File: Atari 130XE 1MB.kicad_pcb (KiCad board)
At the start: 2 copper layers, 324 x 204 mm, 348 parts, among them J1 SIO, J10 Mem_on_off, J100 cond, J101 cond, J102 pin, J103 pin, J104 pin, J105 pin, J106 pin, J107 pin, J2 Video, J201 Diagnostic, J202 Diag, J210 Diag, J211 Conn_01x02, J24 Cartridge, J4 Expansion, J5 Joystick_Port, J6 Joystick_Port, J7 Power, J8 Keyboard, M1 Modulator, Q1 2N3904, Q2 2N3904, Q3 2N3904, Q4 2N3906, Q6 2N3904, SW1 Switch_power_on, U1 LM358, U10 DRAM_4464, U100 74LS157, U17 GTIA, U18 74LS08, U19 LM555, U2 74LS138, U20 4050, U21 74LS74, U22 POKEY, U23 PIA, U24 CD4051B, U25 CD4051B, U3 MMU, U4 27C010, U40 GAL20V8_DIP, U41 74LS157, U42 74LS175, U43 DRAM_1MB_4bit, U44 DRAM_1MB_4bit, U5 27C010, U6 Freddie, U7 Antic, U8 Sally, U9 DRAM_4464, Y1 Crystal, Y2 4,43 MHz

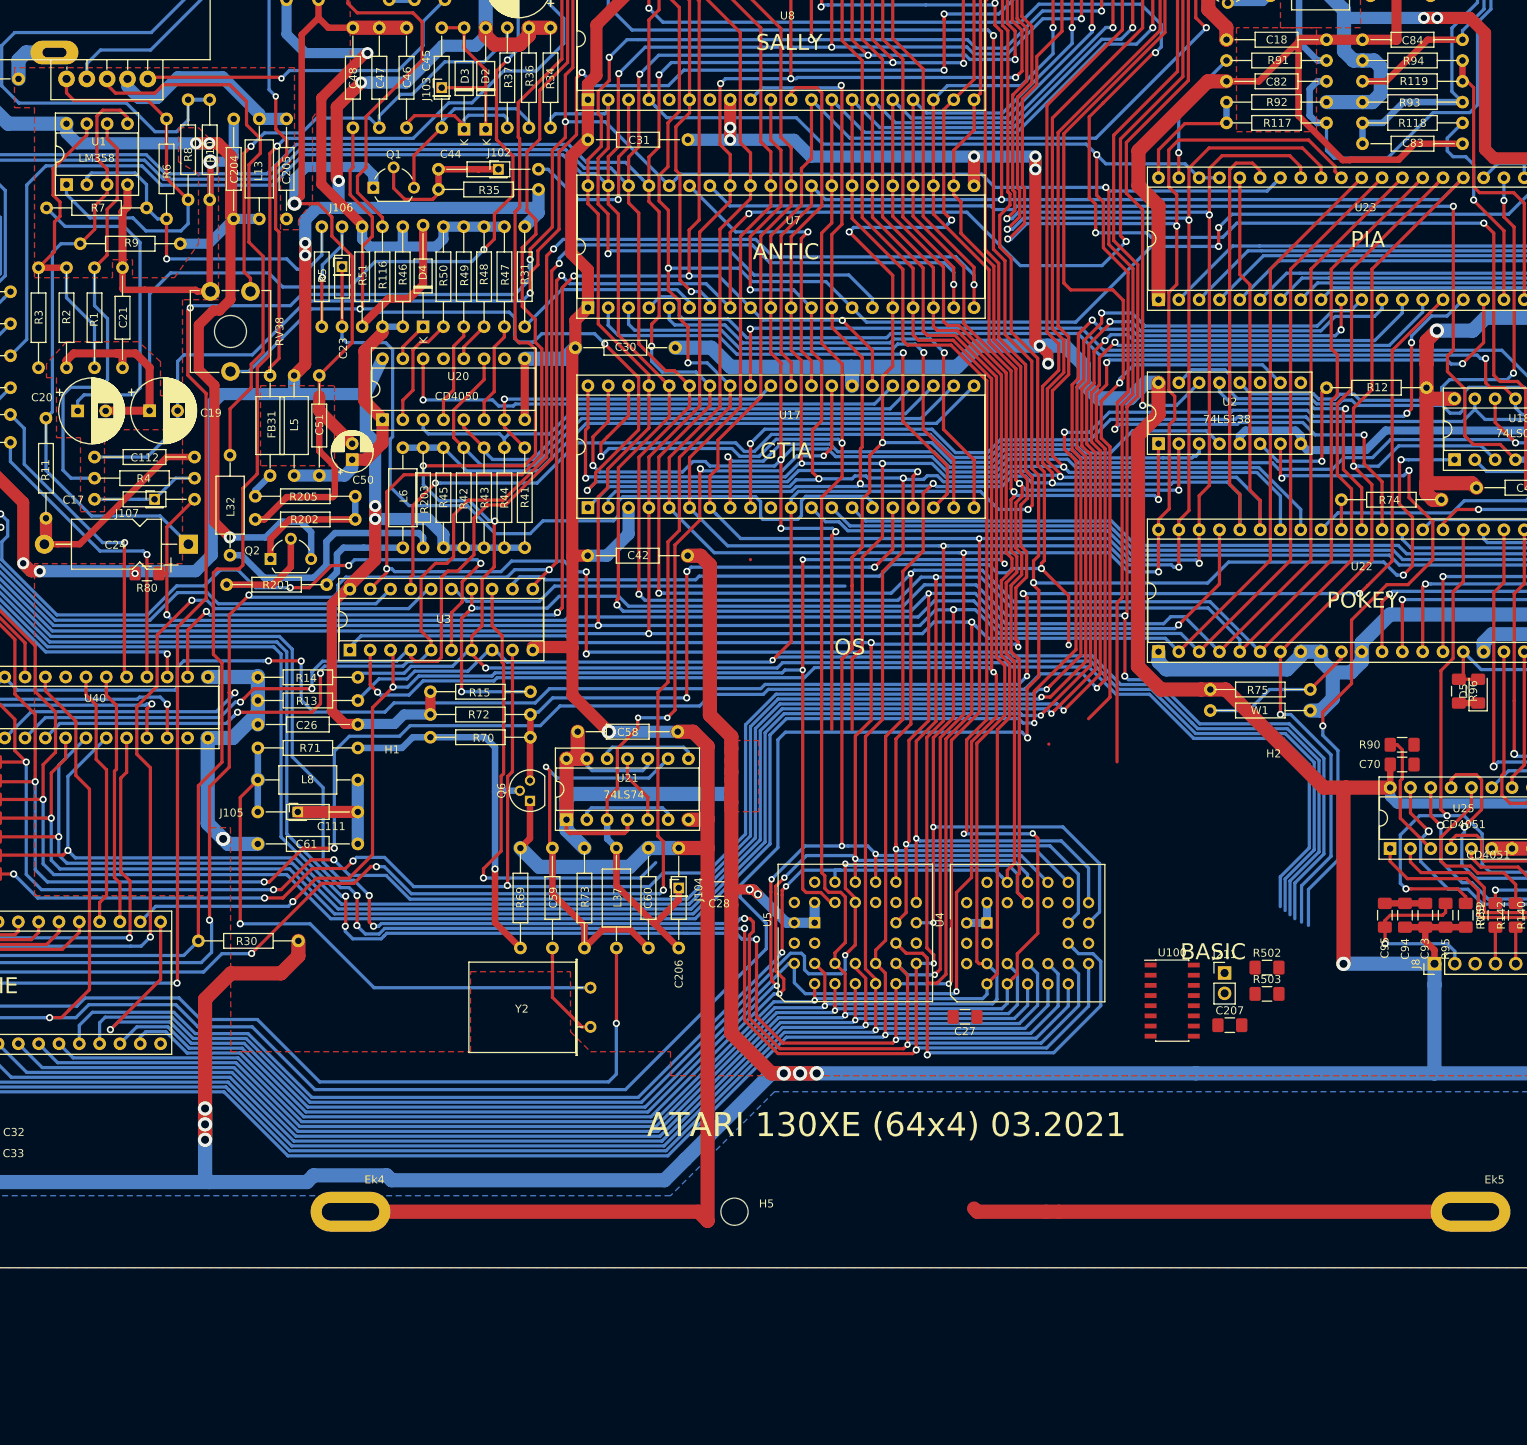
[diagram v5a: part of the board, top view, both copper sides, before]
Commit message: Add Basci and SO PLCC
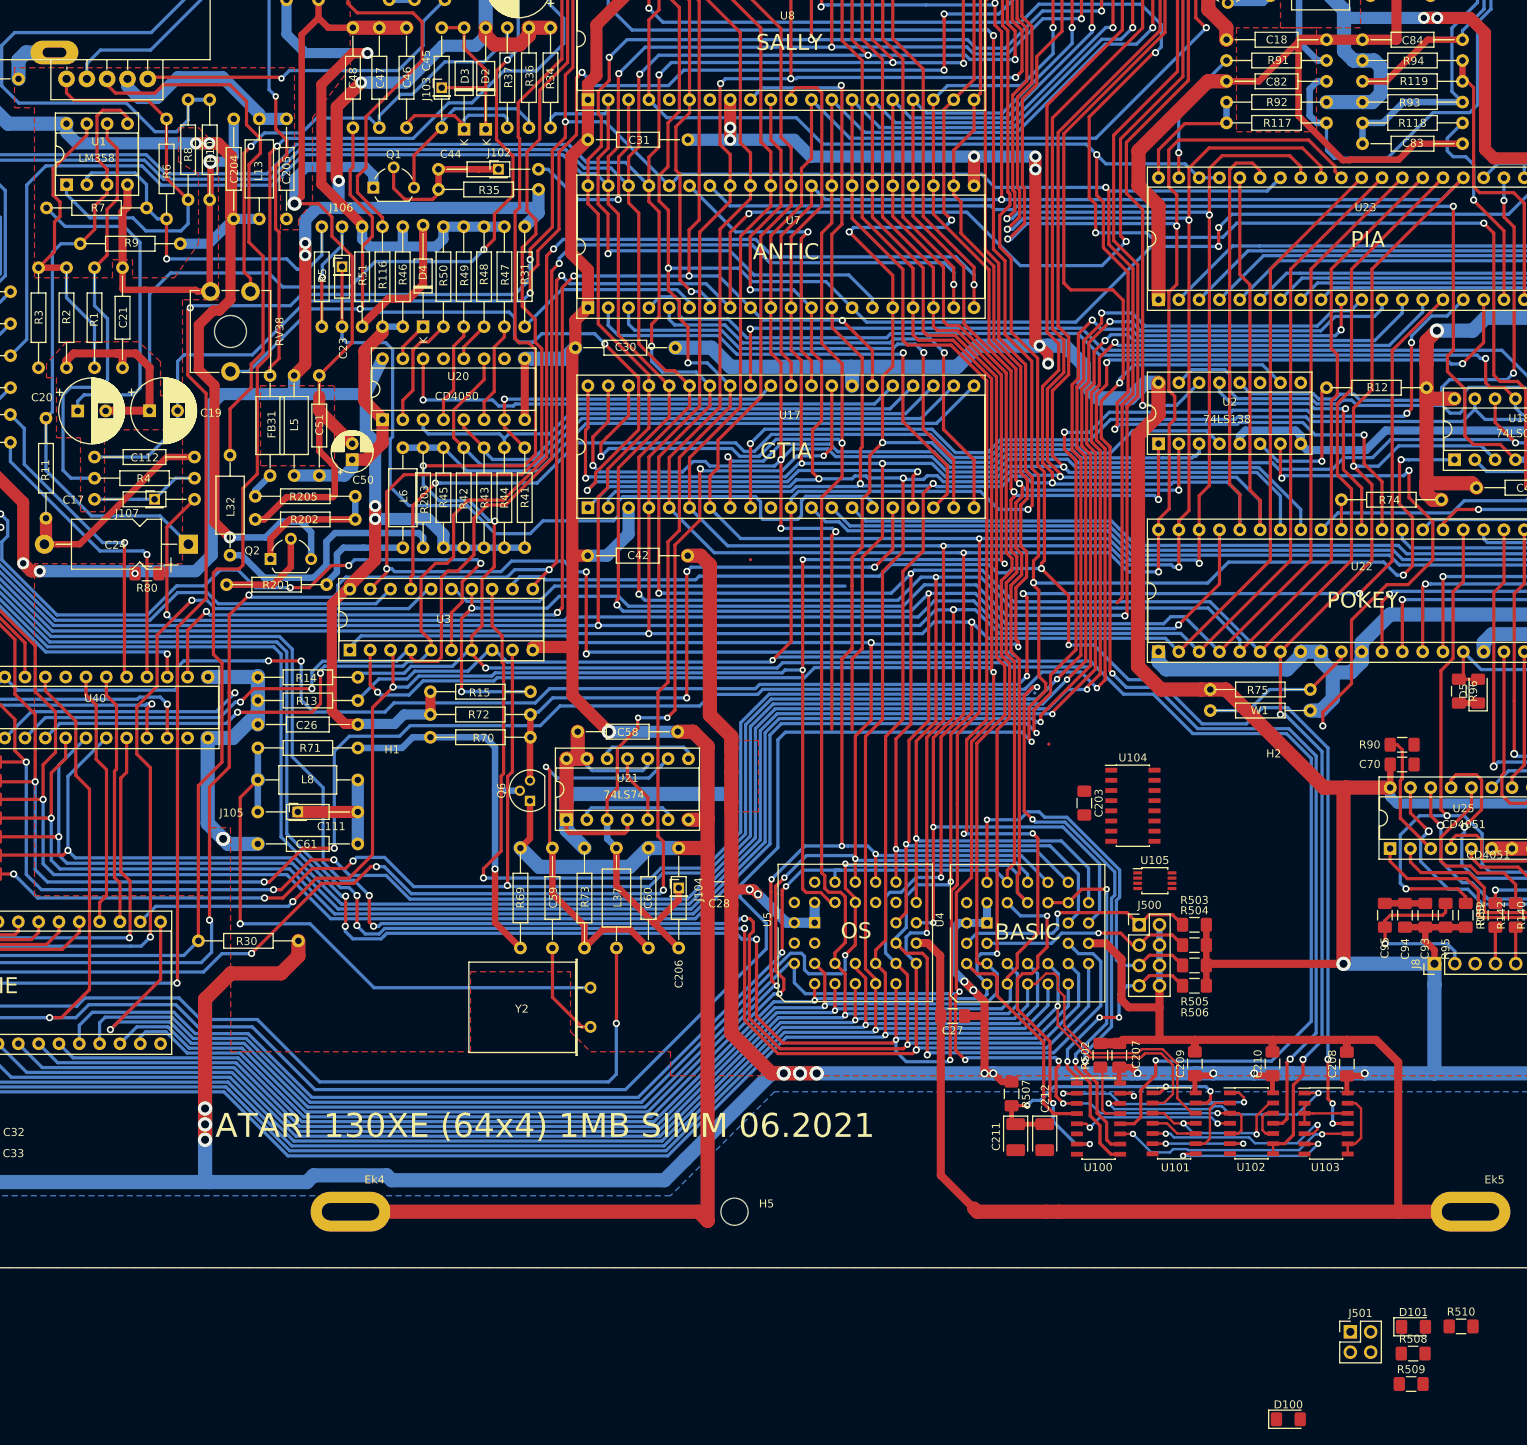
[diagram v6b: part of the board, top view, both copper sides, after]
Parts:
- removed J211: Conn_01x02, Connector_PinHeader_2.54mm:PinHeader_1x02_P2.54mm_Vertical
- added C203: 1uF, Capacitor_SMD:C_1206_3216Metric_Pad1.42x1.75mm_HandSolder, F.Cu at (240.6, 188.8)
- added C208: 100nF, Capacitor_SMD:C_1206_3216Metric_Pad1.42x1.75mm_HandSolder, F.Cu at (273.4, 221.4)
- added C209: 100nF, Capacitor_SMD:C_1206_3216Metric_Pad1.42x1.75mm_HandSolder, F.Cu at (254.4, 221.4)
- added C210: 100nF, Capacitor_SMD:C_1206_3216Metric_Pad1.42x1.75mm_HandSolder, F.Cu at (264.1, 221.4)
- added C211: 22uF, Capacitor_Tantalum_SMD:CP_EIA-3528-21_Kemet-B_Pad1.50x2.35mm_HandSolder, F.Cu at (232.0, 230.6)
- added C212: 4u7, Capacitor_Tantalum_SMD:CP_EIA-3528-21_Kemet-B_Pad1.50x2.35mm_HandSolder, F.Cu at (235.7, 230.6)
- added D100: 1N4148, Diode_SMD:D_1206_3216Metric_Pad1.42x1.75mm_HandSolder, F.Cu at (266.1, 265.8)
- added D101: 1N4148, Diode_SMD:D_1206_3216Metric_Pad1.42x1.75mm_HandSolder, F.Cu at (281.8, 254.3)
- added J500: Basic_sel, Connector_PinHeader_2.54mm:PinHeader_2x04_P2.54mm_Vertical, F.Cu at (247.5, 204.0)
- added J501: TPP_sel, Connector_PinHeader_2.54mm:PinHeader_2x02_P2.54mm_Vertical, F.Cu at (273.9, 254.9)
- added R504: 10k, Resistor_SMD:R_1206_3216Metric_Pad1.42x1.75mm_HandSolder, F.Cu at (254.4, 206.6)
- added R505: 10k, Resistor_SMD:R_1206_3216Metric_Pad1.42x1.75mm_HandSolder, F.Cu at (254.4, 209.1)
- added R506: 10k, Resistor_SMD:R_1206_3216Metric_Pad1.42x1.75mm_HandSolder, F.Cu at (254.4, 211.6)
- added R507: 1k2, Resistor_SMD:R_1206_3216Metric_Pad1.42x1.75mm_HandSolder, F.Cu at (231.5, 225.1)
- added R508: 4k7, Resistor_SMD:R_1206_3216Metric_Pad1.42x1.75mm_HandSolder, F.Cu at (281.7, 257.6)
- added R509: 4k7, Resistor_SMD:R_1206_3216Metric_Pad1.42x1.75mm_HandSolder, F.Cu at (281.5, 261.4)
- added R510: 10k, Resistor_SMD:R_1206_3216Metric_Pad1.42x1.75mm_HandSolder, F.Cu at (287.7, 254.2)
- added U101: 74LS74, Package_SO:SOIC-14_3.9x8.7mm_P1.27mm, F.Cu at (251.8, 228.8)
- added U102: 74HC02, Package_SO:SOIC-14_3.9x8.7mm_P1.27mm, F.Cu at (261.5, 228.8)
- added U103: 74HC02, Package_SO:SOIC-14_3.9x8.7mm_P1.27mm, F.Cu at (270.8, 228.9)
- added U104: 74LS157, Package_SO:SOIC-16_3.9x9.9mm_P1.27mm, F.Cu at (246.7, 189.1)
- added U105: 74LVC2G74, Package_SO:TSSOP-8_3x3mm_P0.65mm, F.Cu at (249.4, 198.5)
- moved R502 23.5 mm to (242.6, 220.3), turned to 90 degrees
- moved U100 17.4 mm to (242.4, 228.2)
- moved C207 14.3 mm to (245.0, 220.3), turned to 90 degrees
- moved R503 12.5 mm to (254.4, 204.0), turned to 180 degrees
- moved C27 1.55 mm to (224.2, 215.4)
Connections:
- R503 pad 2: Net-(J211-Pad1) -> A16_sel
- U100 pad 1: Net-(J211-Pad1) -> Net-(J500-Pad7)
- U100 pad 11: (no net) -> Net-(U100-Pad11)
- U100 pad 12: (no net) -> RD5
- U100 pad 14: (no net) -> Net-(U100-Pad14)
- U100 pad 2: (no net) -> Net-(U100-Pad2)
- U100 pad 5: (no net) -> Net-(U100-Pad5)
- U100 pad 6: +5VA -> GND
- U2 pad 9: (no net) -> D6XX
- U4 pad 2: (no net) -> A16_sel
- U4 pad 29: (no net) -> A14_sel
- U4 pad 3: (no net) -> A15_sel
- U5 pad 2: (no net) -> Net-(U104-Pad12)
- U5 pad 29: (no net) -> Net-(U104-Pad7)
- U5 pad 3: (no net) -> Net-(U104-Pad9)
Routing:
- net BASIC: track 60.5 -> 194.3 mm, vias 1 -> 4
- net GND: track 1397.5 -> 1527.7 mm, vias 33 -> 34
- net S5: track 177.4 -> 265.9 mm, vias 3 -> 6
- net +5VA: track 1963.4 -> 2036.6 mm, vias 33 -> 41
- net CCTL: track 177.4 -> 249.3 mm, vias 4 -> 6
- net S4: track 360.5 -> 296.2 mm
- net MPD: track 332.8 -> 274.5 mm, vias 5 -> 4
- net A12: track 401.3 -> 456.7 mm, vias 5 -> 9
- net RD4: track 355.3 -> 303.4 mm
- net A14_sel: track 0.00 -> 48.8 mm, vias 0 -> 1
- net Net-(U100-Pad9): track 0.00 -> 45.8 mm, vias 0 -> 2
- net RD5: track 294.8 -> 339.4 mm, vias 5 -> 6
- net Net-(U100-Pad7): track 0.00 -> 42.8 mm, vias 0 -> 3
- net Net-(C211-Pad1): track 0.00 -> 37.3 mm, vias 0 -> 3
- net A3: track 432.1 -> 466.9 mm
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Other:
- board text added: "ATARI 130XE (64x4) 1MB SIMM 06.2021"
- board text removed: "ATARI 130XE (64x4) 03.2021"

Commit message: Final modification
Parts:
- added C160: 1n, Capacitor_SMD:C_1206_3216Metric_Pad1.42x1.75mm_HandSolder, F.Cu at (118.9, 83.9)
- added C99: 100nF, Capacitor_SMD:C_1206_3216Metric_Pad1.42x1.75mm_HandSolder, F.Cu at (246.3, 176.1)
- added J11: C, Connector_PinHeader_2.54mm:PinHeader_1x01_P2.54mm_Vertical, F.Cu at (69.7, 73.9)
- added J12: C, Connector_PinHeader_2.54mm:PinHeader_1x01_P2.54mm_Vertical, F.Cu at (69.7, 71.1)
- added J13: C, Connector_PinHeader_2.54mm:PinHeader_1x01_P2.54mm_Vertical, F.Cu at (69.7, 65.6)
- added J14: C, Connector_PinHeader_2.54mm:PinHeader_1x01_P2.54mm_Vertical, F.Cu at (82.9, 73.9)
- added J15: C, Connector_PinHeader_2.54mm:PinHeader_1x01_P2.54mm_Vertical, F.Cu at (82.9, 71.1)
- added J16: C, Connector_PinHeader_2.54mm:PinHeader_1x01_P2.54mm_Vertical, F.Cu at (71.5, 85.4)
- added J17: C, Connector_PinHeader_2.54mm:PinHeader_1x01_P2.54mm_Vertical, F.Cu at (71.5, 88.4)
- added J18: C, Connector_PinHeader_2.54mm:PinHeader_1x01_P2.54mm_Vertical, F.Cu at (71.5, 94.8)
- added J19: C, Connector_PinHeader_2.54mm:PinHeader_1x01_P2.54mm_Vertical, F.Cu at (71.5, 97.8)
- added J20: C, Connector_PinHeader_2.54mm:PinHeader_1x01_P2.54mm_Vertical, F.Cu at (89.9, 89.3)
- added J21: C, Connector_PinHeader_2.54mm:PinHeader_1x01_P2.54mm_Vertical, F.Cu at (89.9, 92.2)
- added J22: C, Connector_PinHeader_2.54mm:PinHeader_1x01_P2.54mm_Vertical, F.Cu at (89.9, 95.1)
- added J50: Test_signal, Connector_PinHeader_2.54mm:PinHeader_2x05_P2.54mm_Vertical, F.Cu at (64.7, 183.5)
- added J51: To_GND, Connector_PinHeader_2.54mm:PinHeader_1x02_P2.54mm_Vertical, F.Cu at (70.3, 200.4)
- added Q10: PN2222A, Package_TO_SOT_THT:TO-92_Inline, F.Cu at (114.6, 80.0)
- added Q11: PN2222A, Package_TO_SOT_THT:TO-92_Inline, F.Cu at (114.6, 86.2)
- added R100: 10k, Atari:R_Axial_DIN0207_L3.6mm_D2.2mm_P10.16mm_Horizontal, F.Cu at (93.9, 140.3)
- added R101: 10k, Atari:R_Axial_DIN0207_L3.6mm_D2.2mm_P10.16mm_Horizontal, F.Cu at (93.9, 135.2)
- added R102: 10k, Atari:R_Axial_DIN0207_L3.6mm_D2.2mm_P10.16mm_Horizontal, F.Cu at (93.9, 130.1)
- added R103: 10k, Atari:R_Axial_DIN0207_L3.6mm_D2.2mm_P10.16mm_Horizontal, F.Cu at (90.9, 110.8)
- added R104: 10k, Atari:R_Axial_DIN0207_L3.6mm_D2.2mm_P10.16mm_Horizontal, F.Cu at (90.9, 105.7)
- added R105: 10k, Atari:R_Axial_DIN0207_L3.6mm_D2.2mm_P10.16mm_Horizontal, F.Cu at (90.9, 108.2)
- added R106: 10k, Atari:R_Axial_DIN0207_L3.6mm_D2.2mm_P10.16mm_Horizontal, F.Cu at (90.9, 103.1)
- added R107: 10k, Atari:R_Axial_DIN0207_L3.6mm_D2.2mm_P10.16mm_Horizontal, F.Cu at (90.9, 100.6)
- added R160: 33, Resistor_SMD:R_1206_3216Metric_Pad1.42x1.75mm_HandSolder, F.Cu at (118.9, 79.1)
- added R161: 18, Resistor_SMD:R_1206_3216Metric_Pad1.42x1.75mm_HandSolder, F.Cu at (118.9, 81.5)
- added R162: 82, Resistor_SMD:R_1206_3216Metric_Pad1.42x1.75mm_HandSolder, F.Cu at (118.9, 88.6)
- added R163: 180, Resistor_SMD:R_1206_3216Metric_Pad1.42x1.75mm_HandSolder, F.Cu at (118.9, 86.2)
- C10, C2, C3, C79: footprint Capacitor_THT:CP_Axial_L11.0mm_D5.0mm_P18.00mm_Horizontal -> Capacitor_THT:CP_Radial_D7.5mm_P2.50mm
- C18, C81, C82, C83, C84, C96, C97: footprint Atari:C_Axial_L5.1mm_D2.5mm_P12.50mm_Horizontal -> Capacitor_SMD:C_1206_3216Metric_Pad1.42x1.75mm_HandSolder
- C19, C20, C22: footprint Capacitor_THT:CP_Radial_D8.0mm_P3.50mm -> Capacitor_THT:C_Rect_L7.2mm_W7.2mm_P5.00mm_FKS2_FKP2_MKS2_MKP2
- C24: footprint Capacitor_THT:CP_Axial_L11.0mm_D6.0mm_P18.00mm_Horizontal -> Capacitor_THT:CP_Radial_D7.5mm_P2.50mm
- C80: footprint Atari:C_Axial_L5.1mm_D2.5mm_P12.50mm_Horizontal -> Resistor_SMD:R_1206_3216Metric_Pad1.42x1.75mm_HandSolder
- FB10, FB11, L23, L30: footprint Atari:L_Axial_L7.0mm_D3.3mm_P12.50mm_Horizontal_Fastron_MICC -> Inductor_SMD:L_1812_4532Metric_Pad1.30x3.40mm_HandSolder
- R117, R118, R119, R132, R133, R91, R92, R93, R94: footprint Atari:R_Axial_DIN0207_L3.6mm_D2.2mm_P10.16mm_Horizontal -> Resistor_SMD:R_1206_3216Metric_Pad1.42x1.75mm_HandSolder
- moved D100 65.1 mm to (250.3, 202.7), turned to 270 degrees
- moved R508 64.4 mm to (248.0, 202.7), turned to 270 degrees
- moved R509 61.2 mm to (264.3, 202.7), turned to 90 degrees
- moved R510 57.6 mm to (262.0, 202.7), turned to 90 degrees
- moved D101 53.7 mm to (266.6, 202.7), turned to 90 degrees
- moved J501 46.7 mm to (261.2, 209.9), turned to 180 degrees
- moved R133 26.2 mm to (314.3, 124.5)
- moved C16 25.2 mm to (82.4, 95.1), turned to 0 degrees
- moved R132 20.8 mm to (314.3, 126.8)
- moved C3 20.0 mm to (82.4, 79.7), turned to 180 degrees
- moved L23 16.4 mm to (345.1, 122.6)
- moved C18 16.1 mm to (271.4, 83.8), turned to 180 degrees
- moved C79 16.0 mm to (278.5, 80.7)
- moved C2 14.3 mm to (70.2, 79.7)
- moved R33 12.9 mm to (300.7, 131.1), turned to 0 degrees
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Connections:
- net Net-(FB7-Pad1) renamed COMPOSITE_A
- U104 pad 11: PB3 -> A16
- U104 pad 12: Net-(U104-Pad12) -> (no net)
- U104 pad 14: A16 -> GND
- U104 pad 2: GND -> PB3
- U104 pad 4: (no net) -> Net-(U104-Pad4)
- U3 pad 15: (no net) -> OS
- U5 pad 2: Net-(U104-Pad12) -> Net-(U104-Pad9)
- U5 pad 22: (no net) -> OS
- U5 pad 24: (no net) -> OS
- U5 pad 3: Net-(U104-Pad9) -> Net-(U104-Pad4)
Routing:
- net GND: track 1527.7 -> 1711.1 mm, vias 34 -> 70
- net +5VA: track 2036.6 -> 2201.1 mm, vias 41 -> 50
- net RST: track 411.8 -> 551.7 mm, vias 8 -> 10
- net (no net): track 111.9 -> 0.00 mm, vias 3 -> 0
- net OS: track 0.00 -> 109.4 mm, vias 0 -> 2
- net D6XX: track 0.00 -> 108.0 mm, vias 0 -> 5
- net S4: track 296.2 -> 206.0 mm, vias 8 -> 5
- net RD4: track 303.4 -> 224.6 mm, vias 7 -> 6
- net FA14: track 31.5 -> 109.6 mm, vias 0 -> 1
- net FA15: track 32.0 -> 107.7 mm, vias 0 -> 1
- net Net-(J501-Pad3): track 0.00 -> 67.3 mm, vias 0 -> 1
- net Net-(U104-Pad4): track 0.00 -> 61.0 mm, vias 0 -> 2
- net Net-(U104-Pad9): track 0.00 -> 60.5 mm, vias 0 -> 2
- net Net-(U104-Pad7): track 0.00 -> 55.5 mm, vias 0 -> 2
- net AUDIO: track 134.4 -> 90.9 mm, vias 0 -> 3
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- removed copper zone on F.Cu, net +5VA
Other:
- board text added: "1MB/512kB"
- board text added: "4,43 MHz"
- board text added: "74HC02"
- board text added: "74LS157"
- board text added: "74LS175"
- board text added: "74LVC2G74"
- board text added: "A14"
- board text added: "A15"
- board text added: "A16"
- board text added: "Basic on/off"
- board text added: "CAS"
- board text added: "CASINH"
- board text added: "FA14"
- board text added: "FA15"
- board text added: "GAL20V8"
- board text added: "MMU"
- board text added: "O2"
- board text added: "OS on/off"
- board text added: "OSC"
- board text added: "RAS"
- board text added: "REF"
- board text added: "RW"
- board text added: "SIMM 1MB 4 bit"
- board text added: "TTP"
- board text added: "WRT"
- board text added: "on/off"
